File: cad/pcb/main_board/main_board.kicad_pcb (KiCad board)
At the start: 2 copper layers, 70.5 x 56.5 mm, 76 parts, among them J1 USB_B_Micro, J2 Conn_ARM_JTAG_SWD_10, U1 STM32F401R_B-C_Tx, U2 TLV75533PDRVR, Y1 Crystal_GND23

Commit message: Update main_board.kicad_pcb
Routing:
- net /MCU/ADC_IN1: track 34.5 -> 35.0 mm
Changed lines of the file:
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@@
+	)
+	(segment
+		(start 102.7 56)
+		(end 98.3 60.4)
+		(width 0.3)
+		(layer "F.Cu")
+		(net 20)
 	)
 	(segment
@@
 	)
 	(segment
-		(start 98.96 59.74)
-		(end 75.1125 59.74)
+		(start 98.3 60.4)
+		(end 75.7725 60.4)
 		(width 0.3)
 		(layer "F.Cu")
@@
 	)
 	(segment
-		(start 75.1125 59.74)
+		(start 75.7725 60.4)
 		(end 73.9125 58.54)
-		(width 0.3)
-		(layer "F.Cu")
-		(net 20)
-	)
-	(segment
-		(start 102.7 56)
-		(end 98.96 59.74)
 		(width 0.3)
 		(layer "F.Cu")
@@
 	)
 	(segment
+		(start 115.6 80.3125)
+		(end 113.9125 82)
+		(width 0.3)
+		(layer "F.Cu")
+		(net 36)
+	)
+	(segment
 		(start 110.75 63.45)
-		(end 115 67.7)
+		(end 115.6 68.3)
+		(width 0.3)
+		(layer "F.Cu")
+		(net 36)
+	)
+	(segment
+		(start 113.9125 84.54)
+		(end 113.9125 82)
+		(width 1)
+		(layer "F.Cu")
+		(net 36)
+	)
+	(segment
+		(start 115.6 68.3)
+		(end 115.6 80.3125)
 		(width 0.3)
 		(layer "F.Cu")
@@
 	)
 	(segment
-		(start 115 67.7)
-		(end 115 80.9125)
-		(width 0.3)
-		(layer "F.Cu")
-		(net 36)
-	)
-	(segment
-		(start 115 80.9125)
-		(end 113.9125 82)
-		(width 0.3)
-		(layer "F.Cu")
-		(net 36)
-	)
-	(segment
-		(start 113.9125 84.54)
-		(end 113.9125 82)
-		(width 1)
-		(layer "F.Cu")
-		(net 36)
-	)
-	(segment
 		(start 112.0875 82)
 		(end 109 82)
@@
 	)
 	(segment
+		(start 91.2 53)
+		(end 83.2 45)
+		(width 0.3)
+		(layer "F.Cu")
+		(net 40)
+	)
+	(segment
+		(start 103.825 53)
+		(end 91.2 53)
+		(width 0.3)
+		(layer "F.Cu")
+		(net 40)
+	)
+	(segment
+		(start 73.86875 42.54)
+		(end 73.86875 40)
+		(width 1)
+		(layer "F.Cu")
+		(net 40)
+	)
+	(segment
+		(start 83.2 45)
+		(end 76.32875 45)
+		(width 0.3)
+		(layer "F.Cu")
+		(net 40)
+	)
+	(segment
 		(start 76.32875 45)
 		(end 73.86875 42.54)
@@
 	)
 	(segment
-		(start 103.825 53)
-		(end 90.5 53)
-		(width 0.3)
-		(layer "F.Cu")
-		(net 40)
-	)
-	(segment
-		(start 73.86875 42.54)
-		(end 73.86875 40)
-		(width 1)
-		(layer "F.Cu")
-		(net 40)
-	)
-	(segment
-		(start 90.5 53)
-		(end 82.5 45)
-		(width 0.3)
-		(layer "F.Cu")
-		(net 40)
-	)
-	(segment
-		(start 82.5 45)
-		(end 76.32875 45)
-		(width 0.3)
-		(layer "F.Cu")
-		(net 40)
-	)
-	(segment
 		(start 72.04375 40)
 		(end 68.95625 40)
@@
 	)
 	(segment
-		(start 85.3725 52)
+		(start 83.9125 50.7125)
 		(end 83.9125 50.54)
 		(width 0.3)
@@
 	(segment
 		(start 103.825 53.5)
-		(end 86.8725 53.5)
+		(end 86.7 53.5)
 		(width 0.3)
 		(layer "F.Cu")
@@
 	)
 	(segment
-		(start 86.8725 53.5)
-		(end 85.3725 52)
-		(width 0.3)
-		(layer "F.Cu")
+		(start 86.7 53.5)
+		(end 83.9125 50.7125)
+		(width 0.3)
+		(layer "F.Cu")

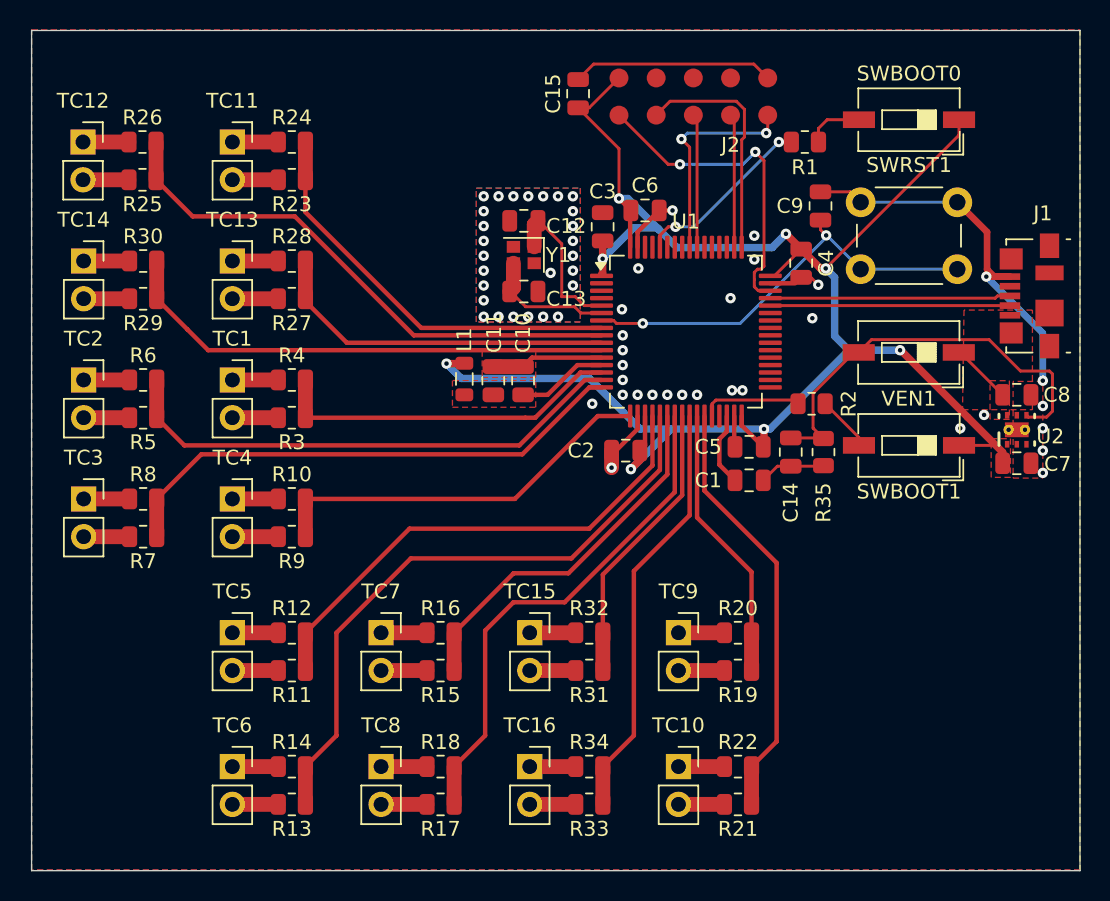
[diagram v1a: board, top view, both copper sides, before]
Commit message: Split Copper Zones Front/Back so that openEMS FreeCAD import tool recognizes them
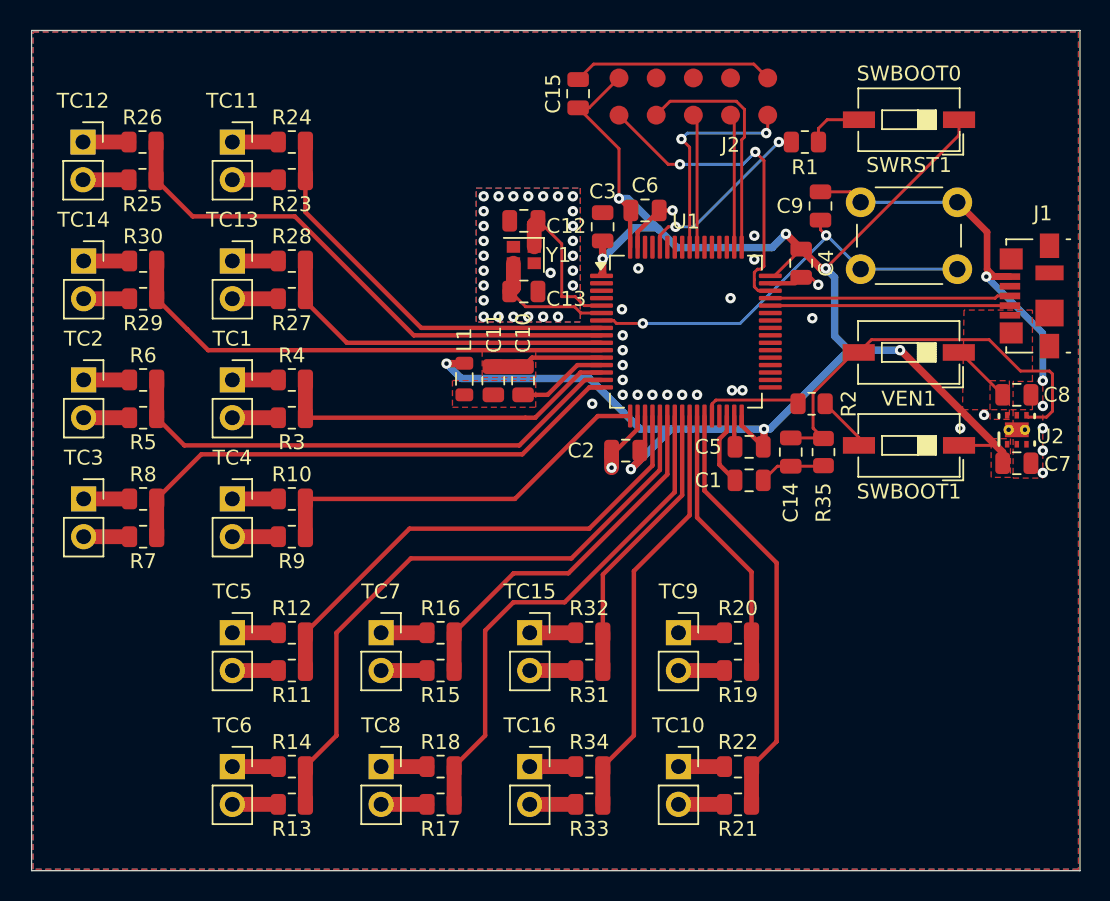
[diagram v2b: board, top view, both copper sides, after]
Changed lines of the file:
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@@
+		(layer "F.Cu")
+		(hatch edge 0.5)
+		(priority 2)
+		(connect_pads yes
+			(clearance 0.2)
+		)
+		(min_thickness 0.25)
+		(filled_areas_thickness no)
+		(fill yes
+			(thermal_gap 0.5)
+			(thermal_bridge_width 0.5)
+		)
+		(polygon
+			(pts
+				(xy 65.6 32.6) (xy 135.9 32.6) (xy 135.9 88.9) (xy 65.6 88.9)
+			)
+		)
+	)
+	(zone
+		(net 2)
+		(net_name "VSS")
 		(layer "F.Cu")
 		(hatch edge 0.5)
@@
 		(layers "F&B.Cu")
 		(hatch edge 0.5)
-		(priority 2)
-		(connect_pads yes
-			(clearance 0.2)
-		)
-		(min_thickness 0.25)
-		(filled_areas_thickness no)
-		(fill yes
-			(thermal_gap 0.5)
-			(thermal_bridge_width 0.5)
-		)
-		(polygon
-			(pts
-				(xy 65.5 32.45) (xy 136 32.45) (xy 136 88.95) (xy 65.5 88.95)
-			)
-		)
-	)
-	(zone
-		(net 2)
-		(net_name "VSS")
-		(layers "F&B.Cu")
-		(hatch edge 0.5)
 		(connect_pads yes
 			(clearance 0.2)
@@
 			)
 		)
+	)
+	(zone
+		(net 2)
+		(net_name "VSS")
+		(layer "B.Cu")
+		(hatch edge 0.5)
+		(priority 2)
+		(connect_pads yes
+			(clearance 0.2)
+		)
+		(min_thickness 0.25)
+		(filled_areas_thickness no)
+		(fill yes
+			(thermal_gap 0.5)
+			(thermal_bridge_width 0.5)
+		)
+		(polygon
+			(pts
+				(xy 65.6 32.6) (xy 135.9 32.6) (xy 135.9 88.9) (xy 65.6 88.9)
+			)
+		)

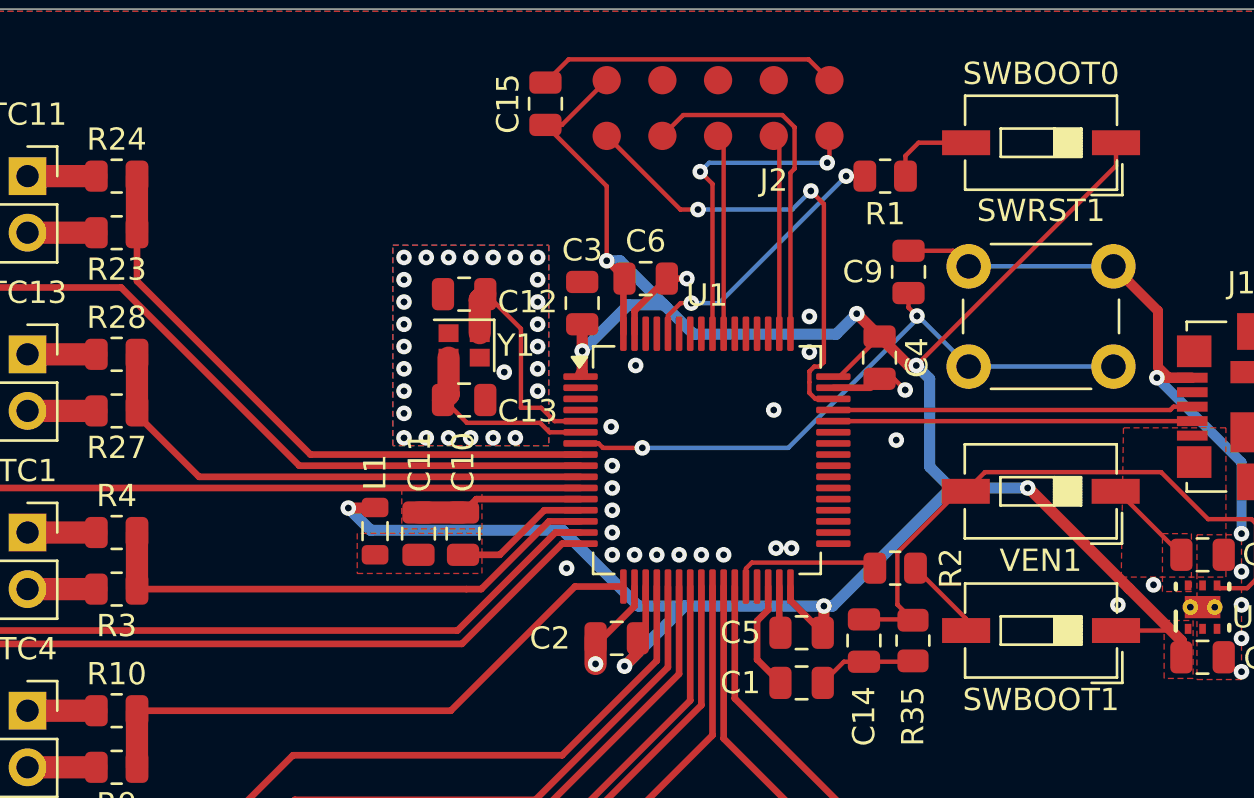
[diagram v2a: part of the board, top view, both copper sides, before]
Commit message: Adding FEA simulation
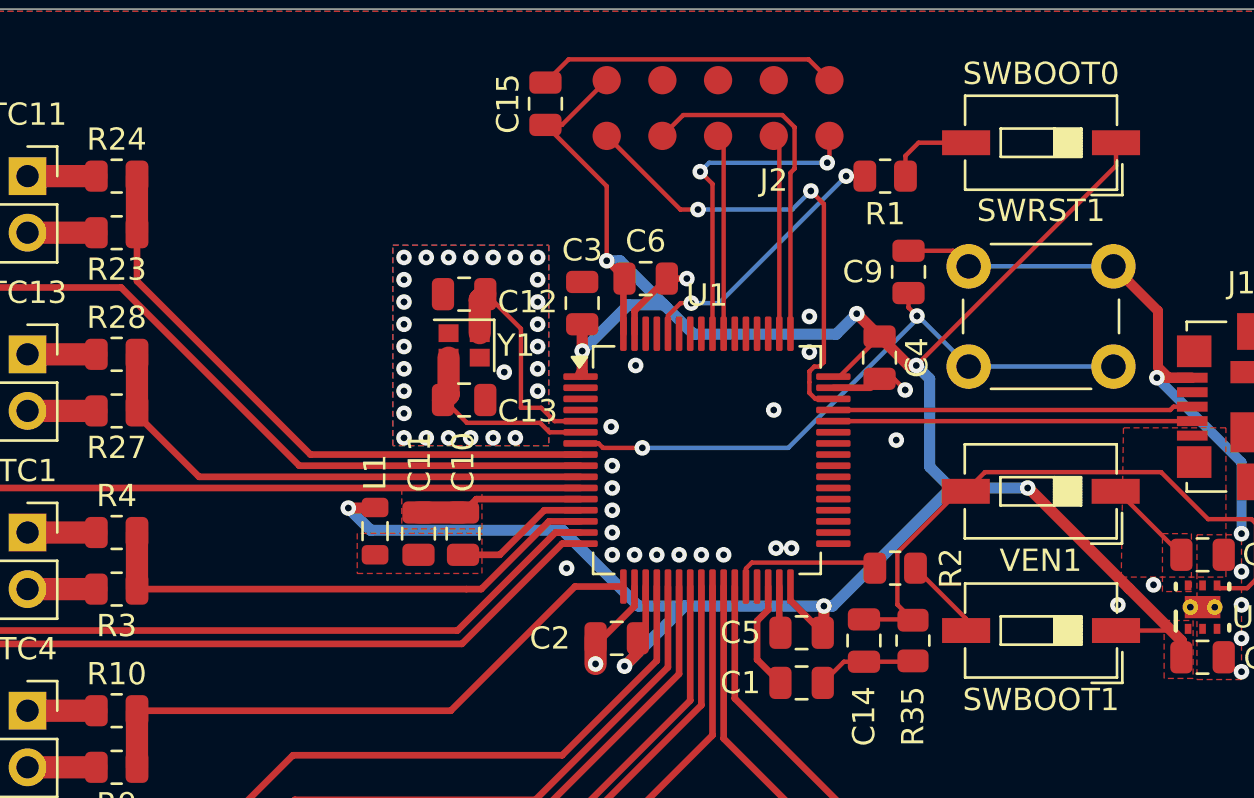
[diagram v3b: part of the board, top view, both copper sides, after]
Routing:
- net VSS: track 103.8 -> 102.1 mm
- net VDD: track 121.8 -> 120.2 mm
- net Net-(U2-EN): track 28.9 -> 28.2 mm
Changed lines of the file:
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@@
-	)
-	(segment
-		(start 117.25 48.95)
-		(end 117.25 49.1)
-		(width 0.2)
-		(layer "F.Cu")
-		(net 2)
 	)
 	(segment
@@
 	)
 	(segment
-		(start 104.80312 60.75)
-		(end 104.8 60.75)
-		(width 0.3)
-		(layer "F.Cu")
-		(net 2)
-	)
-	(segment
 		(start 79 50.54)
 		(end 82.0875 50.54)
@@
 		(end 106.25 59.30312)
 		(width 0.3)
-		(layer "F.Cu")
-		(net 2)
-	)
-	(segment
-		(start 97.9 45.5)
-		(end 97.65 45.25)
-		(width 0.35)
 		(layer "F.Cu")
 		(net 2)
@@
 	)
 	(segment
-		(start 112.75 60.45)
-		(end 112.8 60.5)
-		(width 0.3)
-		(layer "F.Cu")
-		(net 2)
-	)
-	(segment
 		(start 72.0875 58.54)
 		(end 69 58.54)
@@
 	)
 	(segment
-		(start 97.65 45.25)
-		(end 97.65 45.1)
-		(width 0.35)
-		(layer "F.Cu")
-		(net 2)
-	)
-	(segment
 		(start 107.7 44.6)
 		(end 108.6 44.6)
@@
 		(end 79 42.54)
 		(width 1)
-		(layer "F.Cu")
-		(net 2)
-	)
-	(segment
-		(start 117.25 49.1)
-		(end 116.85 49.5)
-		(width 0.2)
 		(layer "F.Cu")
 		(net 2)
@@
 	)
 	(segment
-		(start 118.7125 61.8)
-		(end 118.75 61.7625)
-		(width 0.2)
-		(layer "F.Cu")
-		(net 2)
-	)
-	(segment
 		(start 112.0875 84.54)
 		(end 109 84.54)
@@
 		(net 2)
 	)
-	(segment
-		(start 99.3 49.9)
-		(end 99.55 50.15)
-		(width 0.35)
-		(layer "F.Cu")
-		(net 2)
-	)
 	(via
 		(at 95.9 51.75)
@@
 	)
 	(segment
-		(start 115.175 49)
-		(end 115.45 49)
-		(width 0.2)
-		(layer "F.Cu")
-		(net 3)
-	)
-	(segment
 		(start 117.25 47.2)
 		(end 116.225 46.175)
@@
 	)
 	(segment
-		(start 114.75 60.45)
-		(end 114.7 60.5)
-		(width 0.5)
-		(layer "F.Cu")
-		(net 3)
-	)
-	(segment
-		(start 105.75 44.65)
-		(end 105.8 44.6)
-		(width 0.3)
-		(layer "F.Cu")
-		(net 3)
-	)
-	(segment
 		(start 105 35.6925)
 		(end 102.9925 37.7)
@@
 	)
 	(segment
-		(start 113.25 58.425)
-		(end 113.25 59.05)
-		(width 0.3)
-		(layer "F.Cu")
-		(net 3)
-	)
-	(segment
 		(start 113.25 59.05)
 		(end 114.7 60.5)
@@
 	)
 	(segment
-		(start 106.75 60.7)
-		(end 106.7 60.75)
-		(width 0.3)
-		(layer "F.Cu")
-		(net 3)
-	)
-	(segment
 		(start 105.8 62)
 		(end 106.4 61.4)
@@
 	)
 	(segment
-		(start 94.575 54.9)
-		(end 94.6 54.875)
-		(width 0.5)
-		(layer "F.Cu")
-		(net 3)
-	)
-	(segment
 		(start 130.8 60.86)
 		(end 128.445 58.505)
@@
 	)
 	(segment
-		(start 106.75 60.4)
-		(end 106.4 60.75)
-		(width 0.3)
-		(layer "F.Cu")
-		(net 3)
-	)
-	(segment
 		(start 123.94 54)
 		(end 123.9 54)
@@
 	)
 	(segment
-		(start 127.85 54.15)
-		(end 127.95 54.15)
-		(width 0.2)
-		(layer "F.Cu")
-		(net 4)
-	)
-	(segment
 		(start 104.63241 52)
 		(end 104.83241 52.2)
@@
 	)
 	(segment
-		(start 99.55 46.9)
-		(end 99.3 47.15)
-		(width 0.35)
-		(layer "F.Cu")
-		(net 7)
-	)
-	(segment
 		(start 99.55 45.25)
 		(end 101.15 46.85)
@@
 	)
 	(segment
-		(start 118.7125 59.9)
-		(end 118.75 59.9375)
-		(width 0.2)
-		(layer "F.Cu")
-		(net 9)
-	)
-	(segment
-		(start 120.8 54.15)
-		(end 121.12 54.15)
-		(width 0.2)
-		(layer "F.Cu")
-		(net 9)
-	)
-	(segment
 		(start 118.05 56.9)
 		(end 120.8 54.15)
@@
 	)
 	(segment
-		(start 118.75 59.9375)
-		(end 118.75 60.265256)
-		(width 0.2)
-		(layer "F.Cu")
-		(net 9)
-	)
-	(segment
 		(start 129.89 53.29)
 		(end 132 55.4)
@@
 	(segment
 		(start 121.135 38.5)
-		(end 121.135 38.774744)
-		(width 0.2)
-		(layer "F.Cu")
-		(net 14)
-	)
-	(segment
-		(start 121.135 38.5)
 		(end 119 38.5)
 		(width 0.2)
@@
 	)
 	(segment
-		(start 117.0375 57.6)
-		(end 116.7875 57.35)
-		(width 0.2)
-		(layer "F.Cu")
-		(net 17)
-	)
-	(segment
 		(start 111.51759 57.35)
 		(end 111.25 57.61759)
@@
 	)
 	(segment
-		(start 83.9125 50.7125)
-		(end 83.9125 50.54)
-		(width 0.3)
-		(layer "F.Cu")
-		(net 42)
-	)
-	(segment
 		(start 103.825 53.5)
 		(end 86.7 53.5)
@@
 	)
 	(segment
-		(start 110.25 38.4425)
-		(end 110 38.1925)
-		(width 0.2)
-		(layer "F.Cu")
-		(net 71)
-	)
-	(segment
 		(start 109.75 40.35)
 		(end 109.75 47.075)
@@
 		(layer "F.Cu")
 		(net 85)
-	)
-	(segment
-		(start 112.5 38.1925)
-		(end 112.75 38.4425)
-		(width 0.2)
-		(layer "F.Cu")
-		(net 86)
 	)
 	(segment
@@
 			)
 		)
+	)
+	(zone
+		(net 0)
+		(net_name "")
+		(layer "F.Cu")
+		(hatch edge 0.5)
+		(connect_pads yes
+			(clearance 0)
+		)
+		(min_thickness 0.25)
+		(filled_areas_thickness no)
+		(keepout
+			(tracks not_allowed)
+			(vias not_allowed)
+			(pads not_allowed)
+			(copperpour not_allowed)
+			(footprints allowed)
+		)
+		(fill
+			(thermal_gap 0.5)
+			(thermal_bridge_width 0.5)
+		)
+		(polygon
+			(pts
+				(xy 98.4 48.1) (xy 98.85 48.1) (xy 98.85 46.9) (xy 98.35 46.9) (xy 98.35 48.1)
+			)
+		)

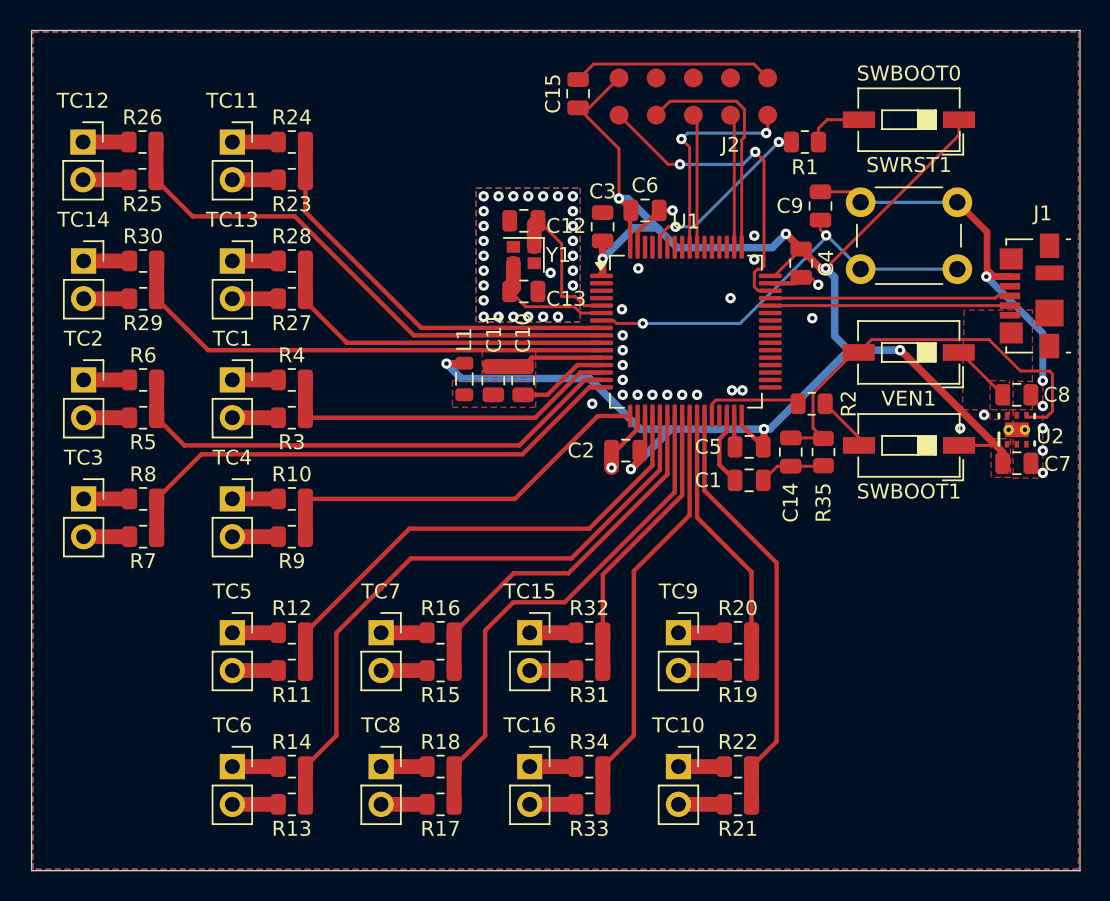
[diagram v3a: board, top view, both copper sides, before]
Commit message: Redoing entire pcb
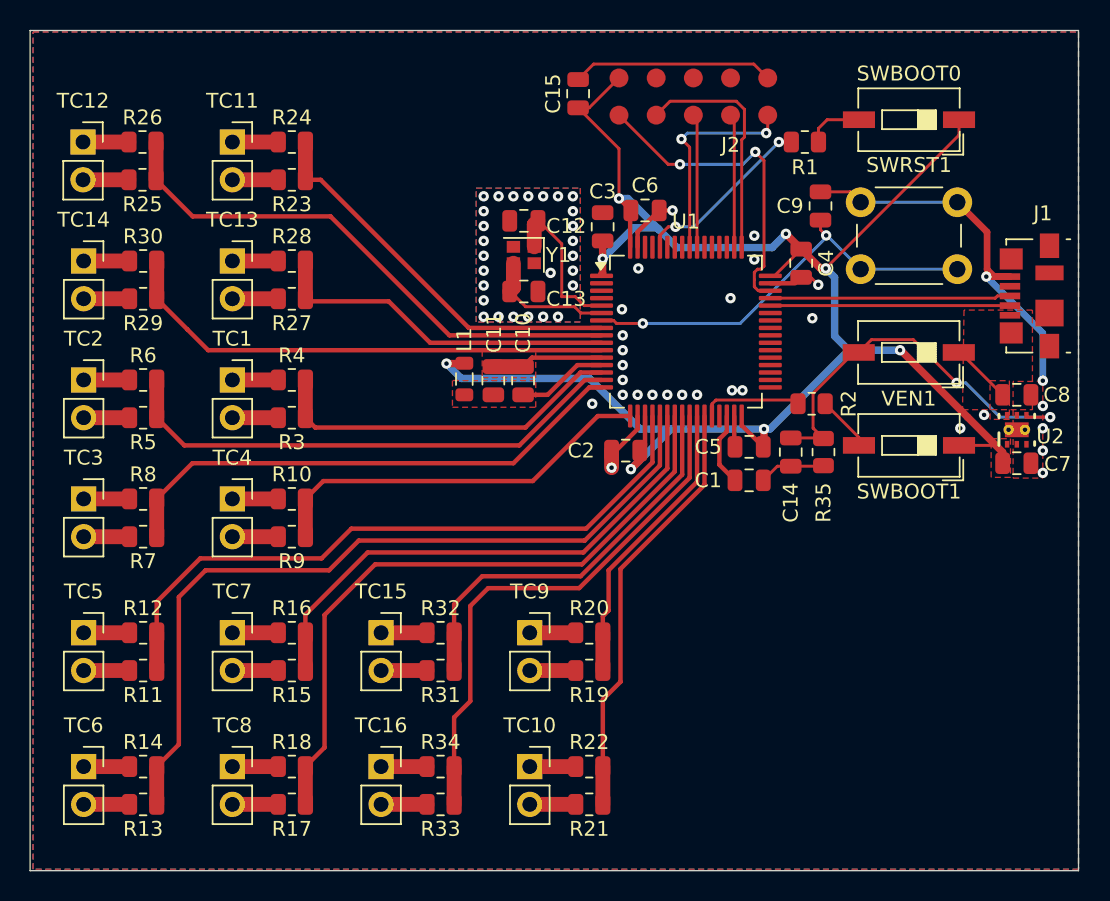
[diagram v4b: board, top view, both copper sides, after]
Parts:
- moved R11 10.0 mm to (73.0, 75.5)
- moved R12 10.0 mm to (73.0, 73.0)
- moved R13 10.0 mm to (73.0, 84.5)
- moved R14 10.0 mm to (73.0, 82.0)
- moved R15 10.0 mm to (83.0, 75.5)
- moved R16 10.0 mm to (83.0, 73.0)
- moved R17 10.0 mm to (83.0, 84.5)
- moved R18 10.0 mm to (83.0, 82.0)
- moved R19 10.0 mm to (103.0, 75.5)
- moved R20 10.0 mm to (103.0, 73.0)
- moved R21 10.0 mm to (103.0, 84.5)
- moved R22 10.0 mm to (103.0, 82.0)
- moved R31 10.0 mm to (93.0, 75.5)
- moved R32 10.0 mm to (93.0, 73.0)
- moved R33 10.0 mm to (93.0, 84.5)
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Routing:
- net /MCU/ADC_IN5: track 42.3 -> 53.9 mm
- net /MCU/ADC_IN4: track 33.9 -> 45.0 mm
- net /MCU/ADC_IN6: track 25.2 -> 35.7 mm
- net /MCU/ADC_IN7: track 34.3 -> 44.6 mm
- net /MCU/ADC_IN14: track 19.3 -> 27.3 mm
- net /MCU/ADC_IN15: track 28.5 -> 36.3 mm
- net Net-(U2-EN): track 28.2 -> 26.4 mm, vias 0 -> 2
- net /MCU/ADC_IN10: track 27.9 -> 26.6 mm
- net /MCU/ADC_IN8: track 18.6 -> 19.7 mm
- net /MCU/ADC_IN0: track 23.7 -> 24.3 mm
